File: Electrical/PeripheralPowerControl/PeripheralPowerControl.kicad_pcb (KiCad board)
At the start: 2 copper layers, 40 x 63 mm, 10 parts, among them J1 Conn_01x03, J2 Screw_Terminal_01x02

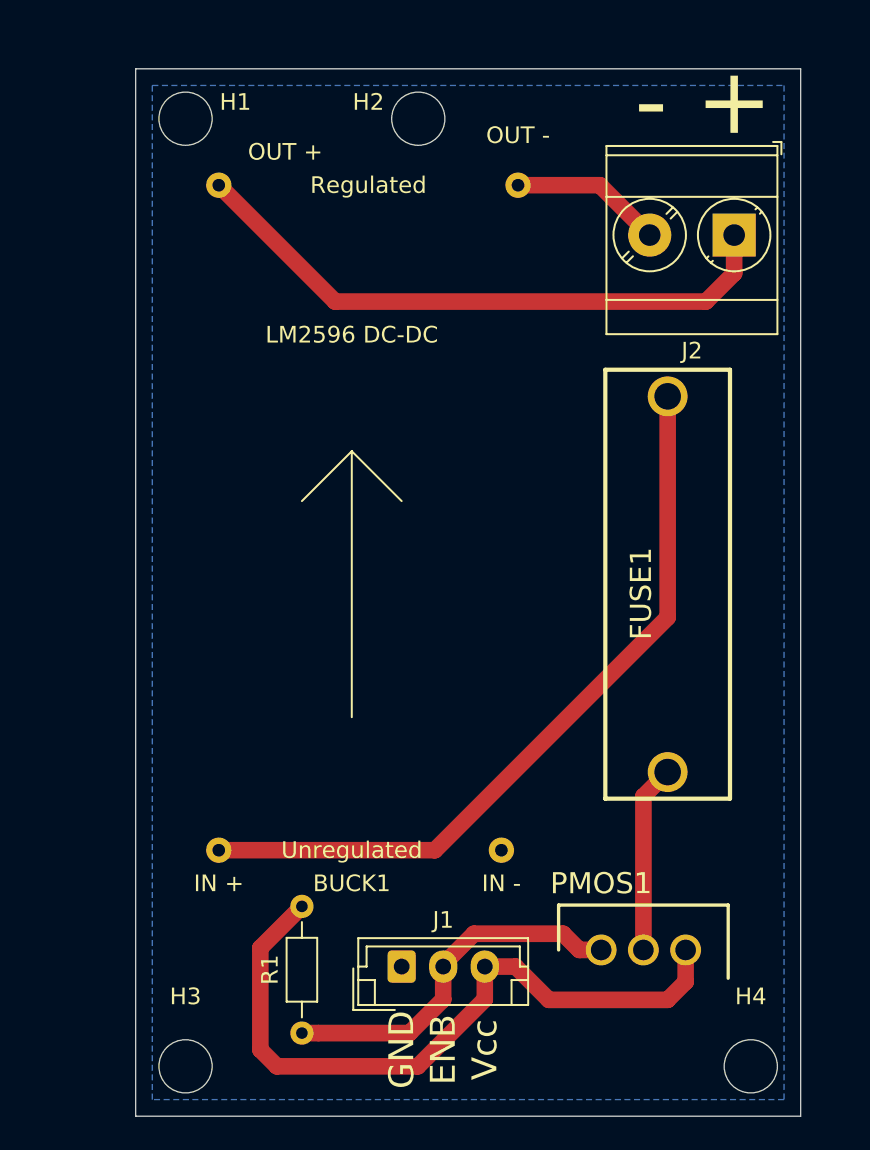
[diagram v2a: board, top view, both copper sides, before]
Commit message: Beefs up traces of peripheral power module to 50 mils - aiming for 10 degC temp rise
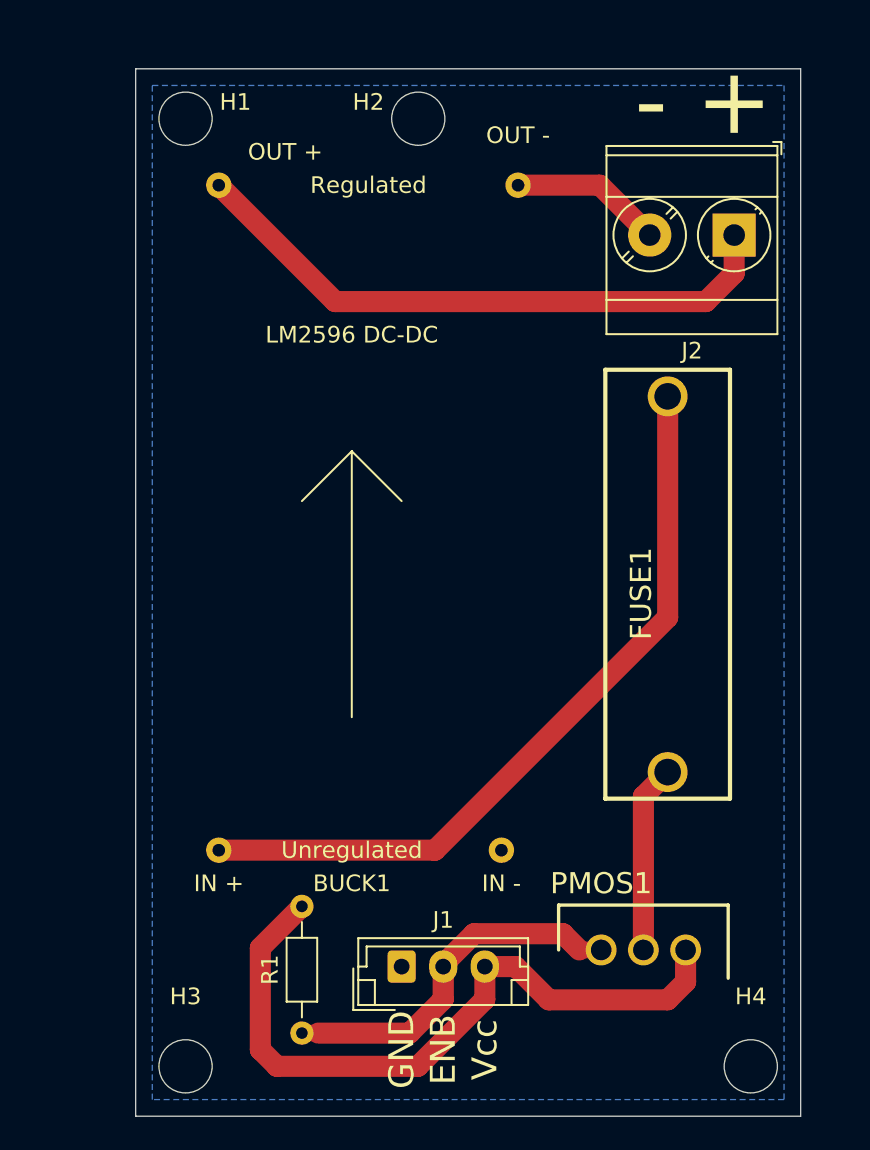
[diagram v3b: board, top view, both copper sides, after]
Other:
- net class Default: trace_width 1 -> 1.27
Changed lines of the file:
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@@
-(kicad_pcb (version 20171130) (host pcbnew "(5.1.4)-1")
+(kicad_pcb (version 20171130) (host pcbnew 5.1.5-52549c5~84~ubuntu16.04.1)
   (general
     (thickness 1.6)
@@
   )
   (setup
-    (last_trace_width 1)
+    (last_trace_width 1.27)
     (trace_clearance 0.2)
     (zone_clearance 0.508)
@@
   (net_class Default "This is the default net class."
     (clearance 0.2)
-    (trace_width 1)
+    (trace_width 1.27)
     (via_dia 0.8)
     (via_drill 0.4)
@@
   (gr_line (start 13 10) (end 53 10) (layer Edge.Cuts) (width 0.05))
   (gr_line (start 13 73) (end 13 10) (layer Edge.Cuts) (width 0.05))
-  (segment (start 49 22.3) (end 49 20) (width 1) (layer F.Cu) (net 1))
-  (segment (start 47.3 24) (end 49 22.3) (width 1) (layer F.Cu) (net 1))
-  (segment (start 25 24) (end 47.3 24) (width 1) (layer F.Cu) (net 1))
-  (segment (start 18 17) (end 25 24) (width 1) (layer F.Cu) (net 1))
-  (segment (start 40.92 17) (end 43.92 20) (width 1) (layer F.Cu) (net 2))
-  (segment (start 36 17) (end 40.92 17) (width 1) (layer F.Cu) (net 2))
-  (segment (start 45 29.7) (end 45 43) (width 1) (layer F.Cu) (net 3))
-  (segment (start 31 57) (end 18 57) (width 1) (layer F.Cu) (net 3))
-  (segment (start 45 43) (end 31 57) (width 1) (layer F.Cu) (net 3))
-  (segment (start 43.54 53.76) (end 45 52.3) (width 1) (layer F.Cu) (net 4))
-  (segment (start 43.54 63) (end 43.54 53.76) (width 1) (layer F.Cu) (net 4))
-  (segment (start 46.08 63) (end 46.08 64.92) (width 1) (layer F.Cu) (net 5))
-  (segment (start 46.08 64.92) (end 45 66) (width 1) (layer F.Cu) (net 5))
-  (segment (start 35.85 64) (end 34 64) (width 1) (layer F.Cu) (net 5))
-  (segment (start 37.85 66) (end 35.85 64) (width 1) (layer F.Cu) (net 5))
-  (segment (start 45 66) (end 37.85 66) (width 1) (layer F.Cu) (net 5))
-  (segment (start 34 65.975) (end 29.975 70) (width 1) (layer F.Cu) (net 5))
-  (segment (start 34 64) (end 34 65.975) (width 1) (layer F.Cu) (net 5))
-  (segment (start 29.975 70) (end 21.5 70) (width 1) (layer F.Cu) (net 5))
-  (segment (start 21.5 70) (end 20.5 69) (width 1) (layer F.Cu) (net 5))
-  (segment (start 20.5 62.88) (end 23 60.38) (width 1) (layer F.Cu) (net 5))
-  (segment (start 20.5 69) (end 20.5 62.88) (width 1) (layer F.Cu) (net 5))
+  (segment (start 49 22.3) (end 49 20) (width 1.27) (layer F.Cu) (net 1))
+  (segment (start 47.3 24) (end 49 22.3) (width 1.27) (layer F.Cu) (net 1))
+  (segment (start 25 24) (end 47.3 24) (width 1.27) (layer F.Cu) (net 1))
+  (segment (start 18 17) (end 25 24) (width 1.27) (layer F.Cu) (net 1))
+  (segment (start 40.92 17) (end 43.92 20) (width 1.27) (layer F.Cu) (net 2))
+  (segment (start 36 17) (end 40.92 17) (width 1.27) (layer F.Cu) (net 2))
+  (segment (start 45 29.7) (end 45 43) (width 1.27) (layer F.Cu) (net 3))
+  (segment (start 31 57) (end 18 57) (width 1.27) (layer F.Cu) (net 3))
+  (segment (start 45 43) (end 31 57) (width 1.27) (layer F.Cu) (net 3))
+  (segment (start 43.54 53.76) (end 45 52.3) (width 1.27) (layer F.Cu) (net 4))
+  (segment (start 43.54 63) (end 43.54 53.76) (width 1.27) (layer F.Cu) (net 4))
+  (segment (start 46.08 63) (end 46.08 64.92) (width 1.27) (layer F.Cu) (net 5))
+  (segment (start 46.08 64.92) (end 45 66) (width 1.27) (layer F.Cu) (net 5))
+  (segment (start 35.85 64) (end 34 64) (width 1.27) (layer F.Cu) (net 5))
+  (segment (start 37.85 66) (end 35.85 64) (width 1.27) (layer F.Cu) (net 5))
+  (segment (start 45 66) (end 37.85 66) (width 1.27) (layer F.Cu) (net 5))
+  (segment (start 34 65.975) (end 29.975 70) (width 1.27) (layer F.Cu) (net 5))
+  (segment (start 34 64) (end 34 65.975) (width 1.27) (layer F.Cu) (net 5))
+  (segment (start 29.975 70) (end 21.5 70) (width 1.27) (layer F.Cu) (net 5))
+  (segment (start 21.5 70) (end 20.5 69) (width 1.27) (layer F.Cu) (net 5))
+  (segment (start 20.5 62.88) (end 23 60.38) (width 1.27) (layer F.Cu) (net 5))
+  (segment (start 20.5 69) (end 20.5 62.88) (width 1.27) (layer F.Cu) (net 5))
   (segment (start 31.5 63.875) (end 31.5 64) (width 1) (layer F.Cu) (net 6))
-  (segment (start 33.35 62.025) (end 31.5 63.875) (width 1) (layer F.Cu) (net 6))
-  (segment (start 38.709782 62.025) (end 33.35 62.025) (width 1) (layer F.Cu) (net 6))
-  (segment (start 39.684782 63) (end 38.709782 62.025) (width 1) (layer F.Cu) (net 6))
+  (segment (start 33.35 62.025) (end 31.5 63.875) (width 1.27) (layer F.Cu) (net 6))
+  (segment (start 38.709782 62.025) (end 33.35 62.025) (width 1.27) (layer F.Cu) (net 6))
+  (segment (start 39.684782 63) (end 38.709782 62.025) (width 1.27) (layer F.Cu) (net 6))
   (segment (start 41 63) (end 39.684782 63) (width 1) (layer F.Cu) (net 6))
   (segment (start 23.989949 68) (end 23 68) (width 1) (layer F.Cu) (net 6))
-  (segment (start 29.475 68) (end 23.989949 68) (width 1) (layer F.Cu) (net 6))
-  (segment (start 31.5 65.975) (end 29.475 68) (width 1) (layer F.Cu) (net 6))
-  (segment (start 31.5 64) (end 31.5 65.975) (width 1) (layer F.Cu) (net 6))
+  (segment (start 29.475 68) (end 23.989949 68) (width 1.27) (layer F.Cu) (net 6))
+  (segment (start 31.5 65.975) (end 29.475 68) (width 1.27) (layer F.Cu) (net 6))
+  (segment (start 31.5 64) (end 31.5 65.975) (width 1.27) (layer F.Cu) (net 6))
   (zone (net 7) (net_name GND) (layer B.Cu) (hatch edge 0.508)
     (connect_pads (clearance 0.508))
